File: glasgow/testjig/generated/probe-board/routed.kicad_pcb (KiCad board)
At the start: 2 copper layers, 75 x 110 mm, 57 parts, among them J1 Connector

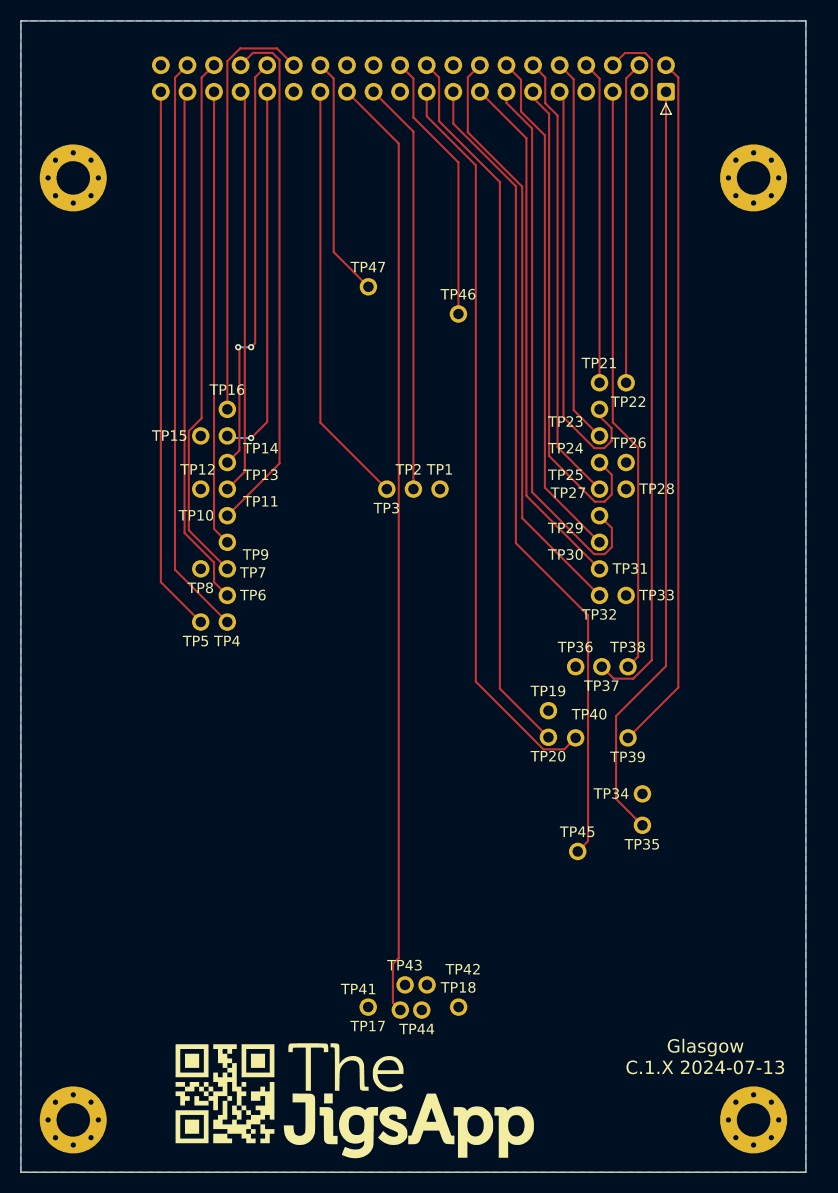
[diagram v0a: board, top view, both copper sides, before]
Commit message: updating labels on glasgow
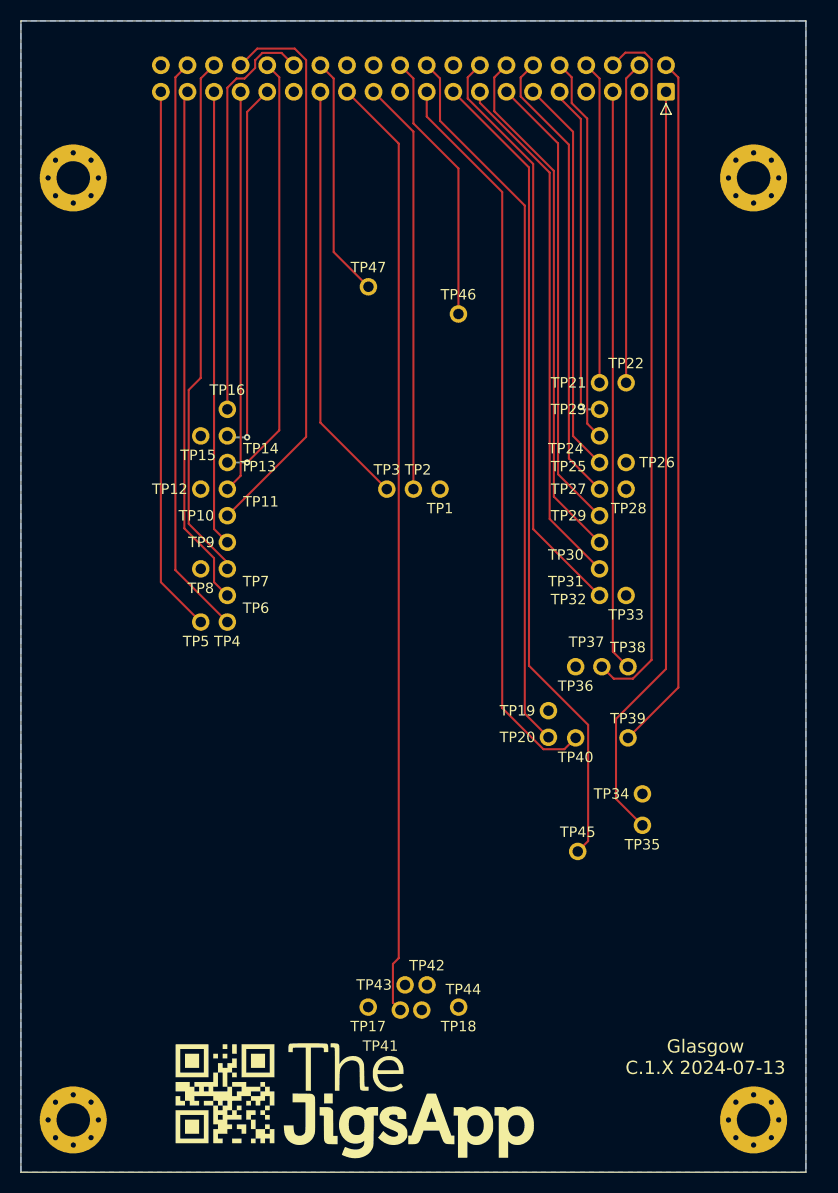
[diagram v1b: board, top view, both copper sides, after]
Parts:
- removed the BOARD at (150.0, 95.0)
- added BOARD: BOARD, tmp9db8qn8v, F.Cu at (150.0, 95.0)
- QR1, QR2: footprint tmplf0ysc42 -> tmpb78doxsu
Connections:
- net /IO_Banks/IO_Buffer_A/VDAC renamed Buffer_A/VDAC
- net /IO_Banks/IO_Buffer_A/VSENSE renamed Buffer_A/VSENSE
- net /IO_Banks/IO_Buffer_A/Z0 renamed Buffer_A/Z0
- net /IO_Banks/IO_Buffer_A/Z1 renamed Buffer_A/Z1
- net /IO_Banks/IO_Buffer_A/Z2 renamed Buffer_A/Z2
- net /IO_Banks/IO_Buffer_A/Z3 renamed Buffer_A/Z3
- net /IO_Banks/IO_Buffer_A/Z4 renamed Buffer_A/Z4
- net /IO_Banks/IO_Buffer_A/Z5 renamed Buffer_A/Z5
- net /IO_Banks/IO_Buffer_A/Z6 renamed Buffer_A/Z6
- net /IO_Banks/IO_Buffer_A/Z7 renamed Buffer_A/Z7
- net /IO_Banks/IO_Buffer_B/VDAC renamed Buffer_B/VDAC
- net /IO_Banks/IO_Buffer_B/VSENSE renamed Buffer_B/VSENSE
- net /IO_Banks/IO_Buffer_B/Z0 renamed Buffer_B/Z0
- net /IO_Banks/IO_Buffer_B/Z1 renamed Buffer_B/Z1
- net /IO_Banks/IO_Buffer_B/Z2 renamed Buffer_B/Z2
- net /IO_Banks/IO_Buffer_B/Z3 renamed Buffer_B/Z3
- net /IO_Banks/IO_Buffer_B/Z4 renamed Buffer_B/Z4
- net /IO_Banks/IO_Buffer_B/Z5 renamed Buffer_B/Z5
- net /IO_Banks/IO_Buffer_B/Z6 renamed Buffer_B/Z6
- net /IO_Banks/IO_Buffer_B/Z7 renamed Buffer_B/Z7
- net /IO_Banks/VIOA renamed VIOA
- net /IO_Banks/VIOB renamed VIOB
- net /IO_Banks/~{SYNC} renamed ~{SYNC}
- net /SCL renamed SCL
- net /SDA renamed SDA
- net /USB_N renamed USB_N
- net /USB_P renamed USB_P
- net /xVBUS renamed xVBUS
- net /~{MR} renamed ~{MR}
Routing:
- net Buffer_B/Z2: track 47.1 -> 38.1 mm
- net Buffer_B/Z4: track 53.1 -> 44.2 mm
- net Buffer_B/Z0: track 40.8 -> 32.8 mm, vias 0 -> 1
- net Buffer_A/Z3: track 50.1 -> 54.0 mm
- net Buffer_A/Z7: track 40.8 -> 39.4 mm
- net Buffer_A/Z5: track 40.4 -> 41.6 mm, vias 2 -> 1
- net Buffer_B/Z3: track 43.1 -> 44.1 mm
- net Buffer_B/Z5: track 49.3 -> 50.2 mm
- net SDA: track 56.3 -> 55.5 mm
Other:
- board text added: "J1 Pins 1:40 1. ~{MR} 2. +5V 3. GND 4. VIOB 5. SDA 6. SCL 7. GND 8. Buffer_B/VSENSE 9. Buffer_B/Z0 10. Buffer_B/Z1 11. Buffer_B/Z2 12. Buffer_B/Z3 13. Buffer_B/Z4 14. Buffer_B/Z5 15. Buffer_B/Z6 16. Buffer_B/Z7 17. +1V2 18. GND 19. +3V3 20. ~{SYNC} 21. GND 22. Buffer_B/VDAC 23. Net-(D12-K) 24. GND 25. xVBUS 26. GND 27. Net-(D13-K) 28. Buffer_A/VDAC 29. GND 30. Buffer_A/Z7 31. Buffer_A/Z6 32. Buff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"
- board text removed: "J1 Pins 1:40 1. /~{MR} 2. +5V 3. GND 4. /IO_Banks/VIOB 5. /SDA 6. /SCL 7. GND 8. /IO_BanB/VSENSE 9. /IO_Banfer_B/Z0 10. /IO_Banfer_B/Z1 11. /IO_Banfer_B/Z2 12. /IO_Banfer_B/Z3 13. /IO_Banfer_B/Z4 14. /IO_Banfer_B/Z5 15. /IO_Banfer_B/Z6 16. /IO_Banfer_B/Z7 17. +1V2 18. GND 19. +3V3 20. /IO_Ban/~{SYNC} 21. GND 22. /IO_Banr_B/VDAC 23. Net-(D12-K) 24. GND 25. /xVBUS 26. GND 27. Net-(D13-K) 28. /IO_Ba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"
